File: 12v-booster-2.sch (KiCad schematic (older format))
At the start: 23 parts, among them J1 Conn_01x06, J2 Conn_01x06, Q1 BSS214NW, Q2 Si4421DY, U1 TPS611781RNW

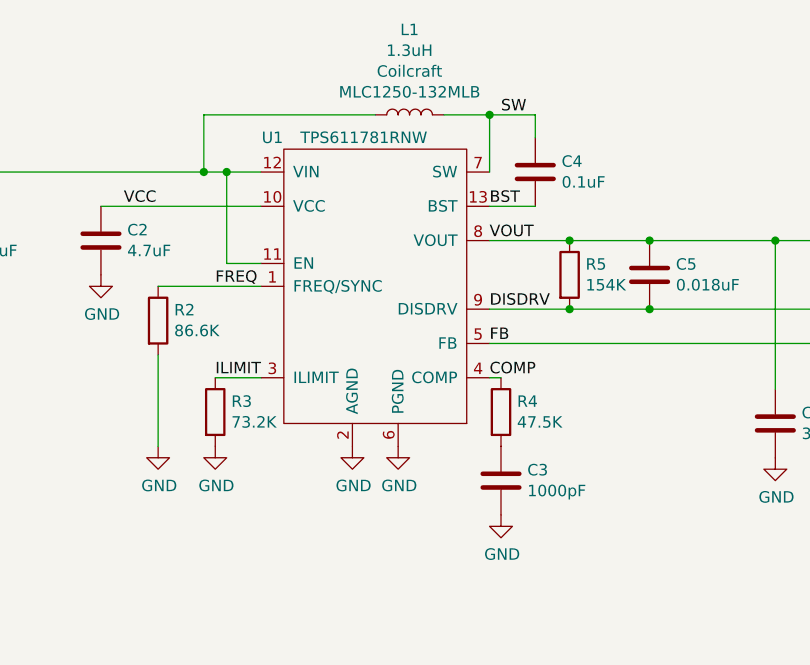
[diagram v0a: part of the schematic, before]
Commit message: Increased output to 2A
Signed-off-by: Aaron Williams <aaron.w2@gmail.com>
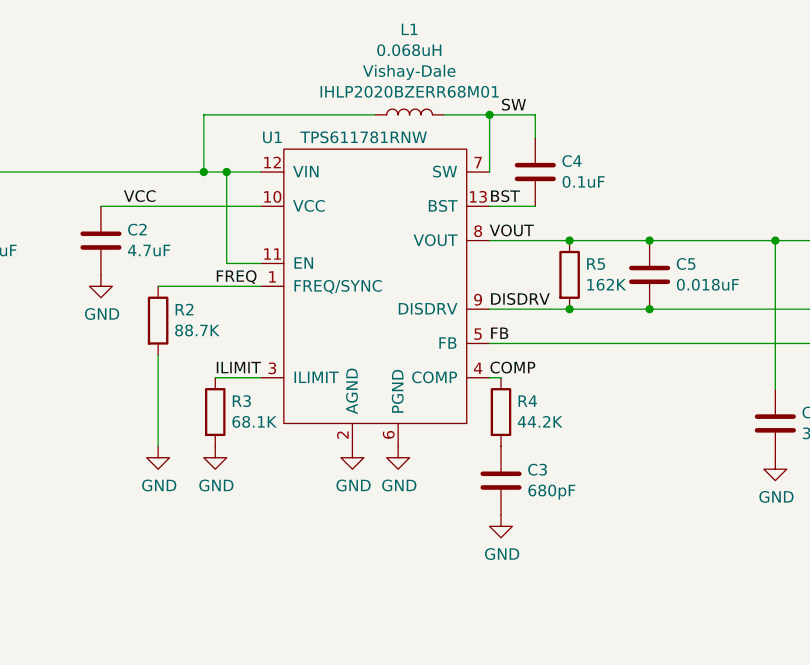
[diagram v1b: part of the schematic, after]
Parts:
- C10: MFR TDK -> Vishay
- C3: value 1000pF -> 680pF; MFR Yageo -> Wurth; MPN CC0603KRX7R9BB102 -> 885012206107; SPN 311-1080-1-ND -> 732-12237-1-ND; SPURL https://www.digikey.com/product-detail/en/yageo/CC0603KRX7R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 -> https://www.digikey.com/product-detail/en/wurth-electronics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
- L1: value 1.3uH -> 0.068uH; footprint Aaron:L_Coilcraft_MLC1250 -> Inductor_SMD:L_Vishay_IHLP-2020; MFR Coilcraft -> Vishay-Dale; MPN MLC1250-132MLB -> IHLP2020BZERR68M01; SPN 994-MLC1250-132MLC -> 541-1086-1-ND; SPR Mouser -> Digikey; SPURL https://www.mouser.com/ProductDetail/Coilcraft/MLC1250-132M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 -> https://www.digikey.com/products/en/inductors-coils-chokes/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
- Q2: footprint Aaron:SO-8_3.9x4.9mm_P1.27mm -> Aaron:SOIC127P600X175-8N
- R2: value 86.6K -> 88.7K; MFR Vishay-Dale -> Yageo; MPN CRCW060386K6FKEA -> RC0603FR-0788K7L; SPN 541-86.6KHCT-ND -> 311-88.7KHRCT-ND; SPURL https://www.digikey.com/product-detail/en/vishay-dale/CRCW0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 -> https://www.digikey.com/product-detail/en/yageo/RC0603FR-07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
- R3: value 73.2K -> 68.1K; MFR Vishay-Dale -> Yageo; MPN CRCW060373K2FKEA -> RC0603FR-0768K1L; SPN 541-73.2KHCT-ND -> 311-68.1KHRCT-ND; SPURL https://www.digikey.com/product-detail/en/vishay-dale/CRCW0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 -> https://www.digikey.com/product-detail/en/yageo/RC0603FR-07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
- R4: value 47.5K -> 44.2K; MPN RC0603FR-0747K5L -> RC0603FR-0744K2L; SPN 311-47.5KHRCT-ND -> 311-44.2KHRCT-ND; SPURL https://www.digikey.com/product-detail/en/yageo/RC0603FR-0747K5L/311-47.5KHRCT-ND/730202 -> https://www.digikey.com/product-detail/en/yageo/RC0603FR-0744K2L/311-44.2KHRCT-ND/730188
- R5: value 154K -> 162K; MFR Yageo -> Vishay-Dale; MPN RC0603FR-07154KL -> TNPW0603162KBEEA; SPN 311-154KHRCT-ND -> 541-3170-1-ND; SPURL https://www.digikey.com/product-detail/en/yageo/RC0603FR-07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 -> https://www.digikey.com/product-detail/en/vishay-dale/TNPW0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
